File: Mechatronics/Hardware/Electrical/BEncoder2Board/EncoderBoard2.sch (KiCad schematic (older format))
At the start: 43 parts, among them J1 Conn_01x08_Male, J2 Conn_01x06_Male, J6 Conn_01x04_Male, Q3 Q_PMOS_GSD, U1 STM32G431CBT6, U2 ITR1802, U3 ITR1802, U4 RN4871, Y1 8Mhz

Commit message: Final PCB
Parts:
- removed J2: Conn_01x06_Male, Encoder:PinHeader_1x06_P2.54mm_Vertical, symbol Connector:Conn_01x06_Male
- added J2: Conn_01x07_Male, Encoder:PinHeader_1x07_P2.54mm_Vertical, symbol Connector:Conn_01x07_Male
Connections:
- wire segments 116 -> 117
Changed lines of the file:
@@
 L power:GND #PWR01
 U 1 1 5F235EDB
-P 7750 3500
-F 0 "#PWR01" H 7750 3250 50  0001 C CNN
-F 1 "GND" H 7700 3350 50  0000 C CNN
-F 2 "" H 7750 3500 50  0001 C CNN
-F 3 "" H 7750 3500 50  0001 C CNN
-	1    7750 3500
-	1    0    0    -1
-$EndComp
-Wire Wire Line
-	7750 3500 8200 3500
+P 7650 3500
+F 0 "#PWR01" H 7650 3250 50  0001 C CNN
+F 1 "GND" H 7600 3350 50  0000 C CNN
+F 2 "" H 7650 3500 50  0001 C CNN
+F 3 "" H 7650 3500 50  0001 C CNN
+	1    7650 3500
+	1    0    0    -1
+$EndComp
+Wire Wire Line
+	7650 3500 8200 3500
 Text Label 8200 3300 2    50   ~ 0
 SWDIO
@@
 Text Label 4950 3500 1    50   ~ 0
 SIGA
-$Comp
-L Connector:Conn_01x06_Male J2
-U 1 1 5EFD316D
-P 8400 3500
-F 0 "J2" H 8372 3382 50  0000 R CNN
-F 1 "Conn_01x06_Male" H 8372 3473 50  0000 R CNN
-F 2 "Encoder:PinHeader_1x06_P2.54mm_Vertical" H 8400 3500 50  0001 C CNN
-F 3 "~" H 8400 3500 50  0001 C CNN
-	1    8400 3500
-	-1   0    0    1
-$EndComp
 Wire Wire Line
 	4350 4100 4350 3300
@@
 Text Label 4050 3600 3    50   ~ 0
 Supply
+$Comp
+L Connector:Conn_01x07_Male J2
+U 1 1 5F0A4213
+P 8400 3400
+F 0 "J2" H 8372 3332 50  0000 R CNN
+F 1 "Conn_01x07_Male" H 8372 3423 50  0000 R CNN
+F 2 "Encoder:PinHeader_1x07_P2.54mm_Vertical" H 8400 3400 50  0001 C CNN
+F 3 "~" H 8400 3400 50  0001 C CNN
+	1    8400 3400
+	-1   0    0    1
+$EndComp
+$Comp
+L power:GND #PWR0111
+U 1 1 5F0A6625
+P 7650 3100
+F 0 "#PWR0111" H 7650 2850 50  0001 C CNN
+F 1 "GND" H 7600 2950 50  0000 C CNN
+F 2 "" H 7650 3100 50  0001 C CNN
+F 3 "" H 7650 3100 50  0001 C CNN
+	1    7650 3100
+	-1   0    0    1
+$EndComp
+Wire Wire Line
+	7650 3100 8200 3100
 $EndSCHEMATC

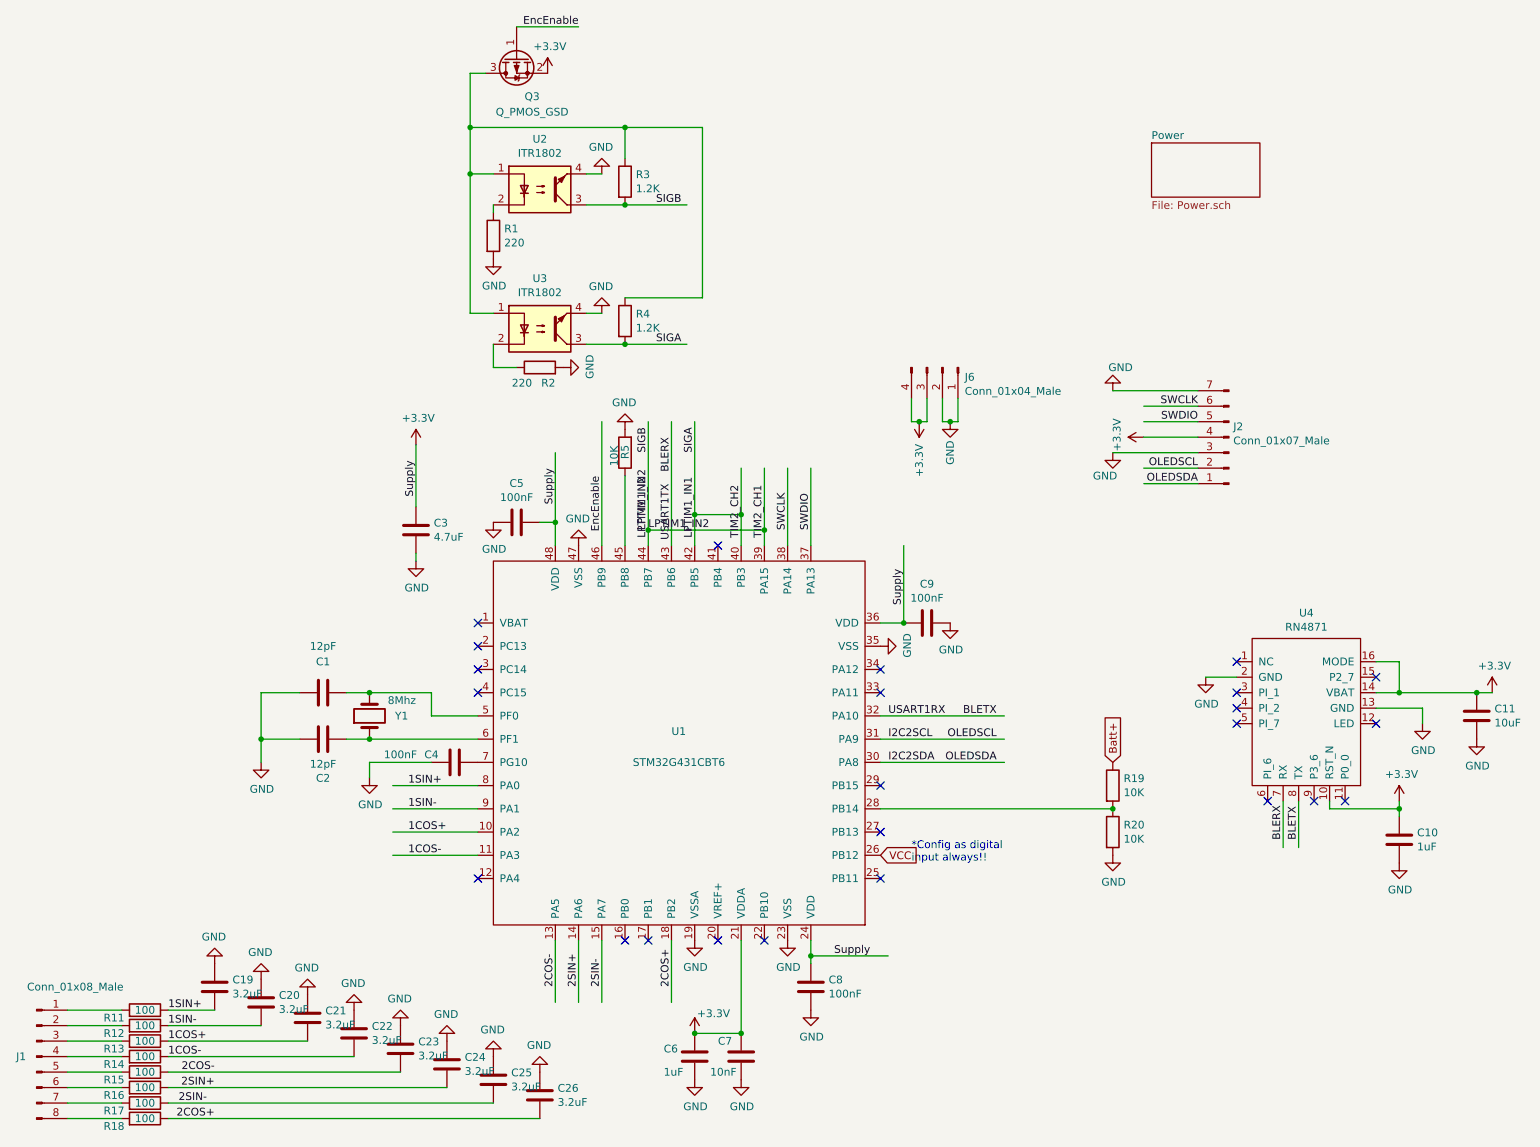
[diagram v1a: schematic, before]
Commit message: Deleted KiBoM & BOM generated
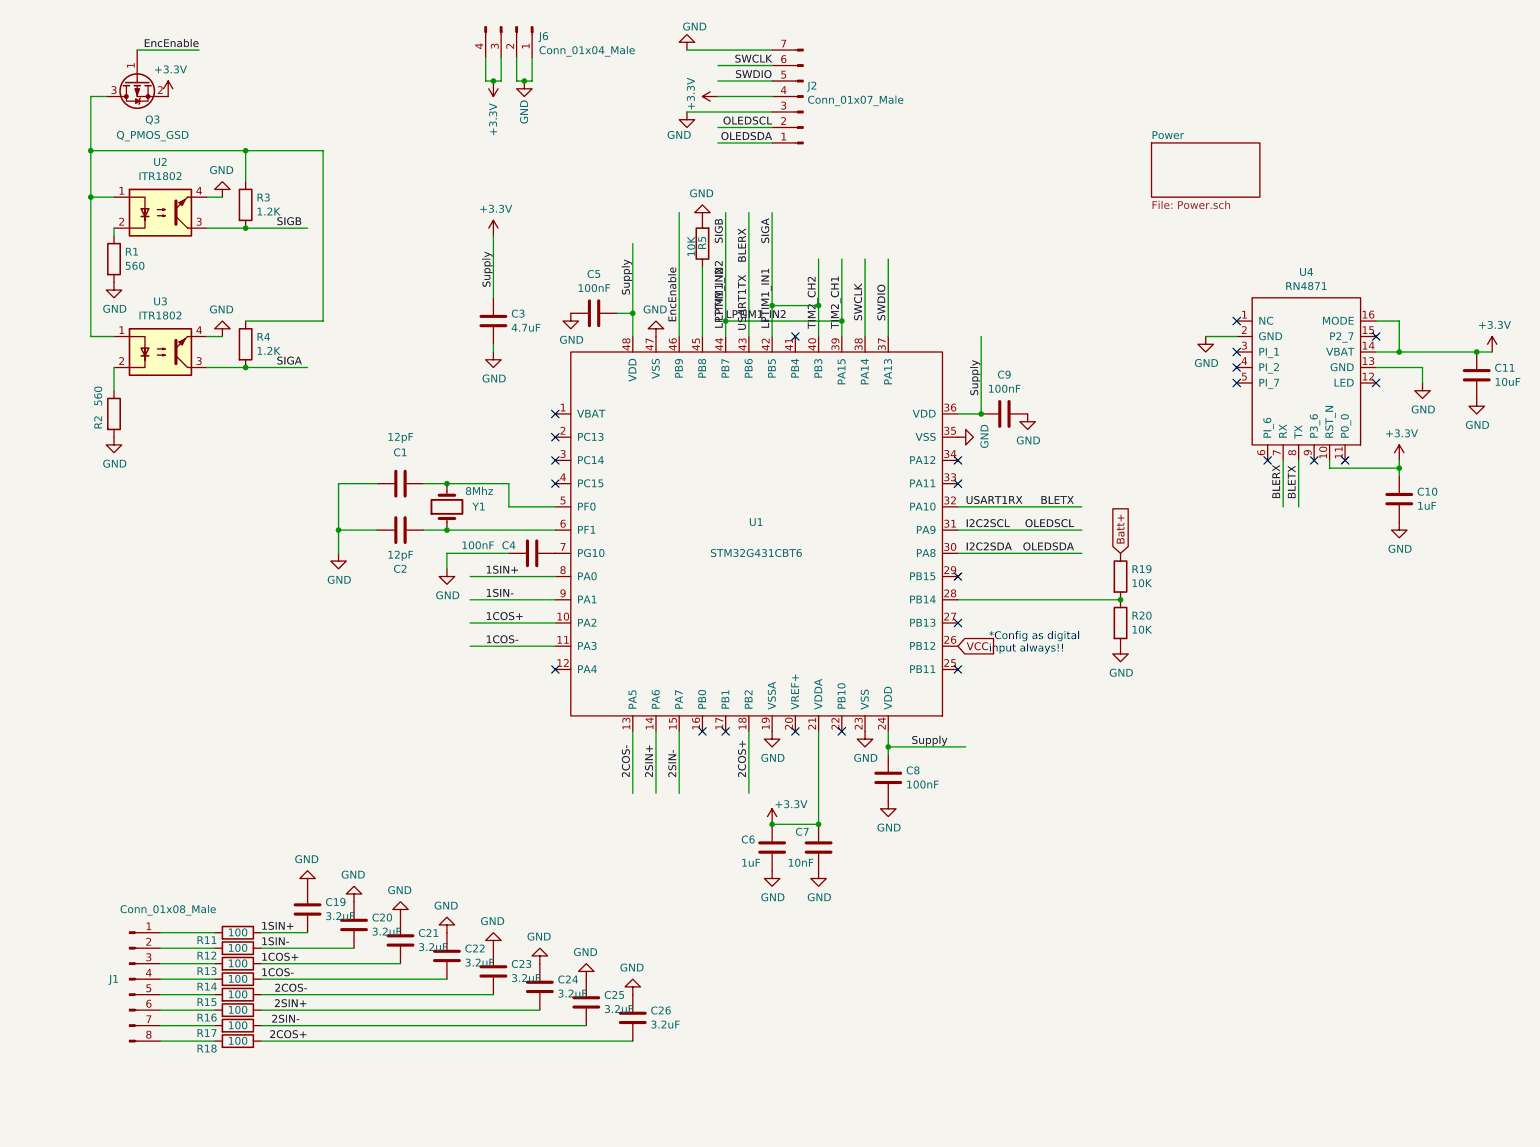
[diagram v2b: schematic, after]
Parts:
- R1, R2: value 220 -> 560
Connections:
- wire segments 117 -> 116
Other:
- moved on the sheet: C1, C10, C11, C19, C2, C20, C21, C22, C23, C24, C25, C26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
